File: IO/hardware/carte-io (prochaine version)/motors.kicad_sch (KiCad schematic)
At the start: 30 parts, among them J4 114020164, J5 114020164, J6 114020164, J7 114020164, J8 TSW-104-07-G-T, J9 TSW-104-07-G-T, U10 CM1293A-04SO, U11 74LVC125APW, U4 CM1293A-04SO, U5 TXU0104PWR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

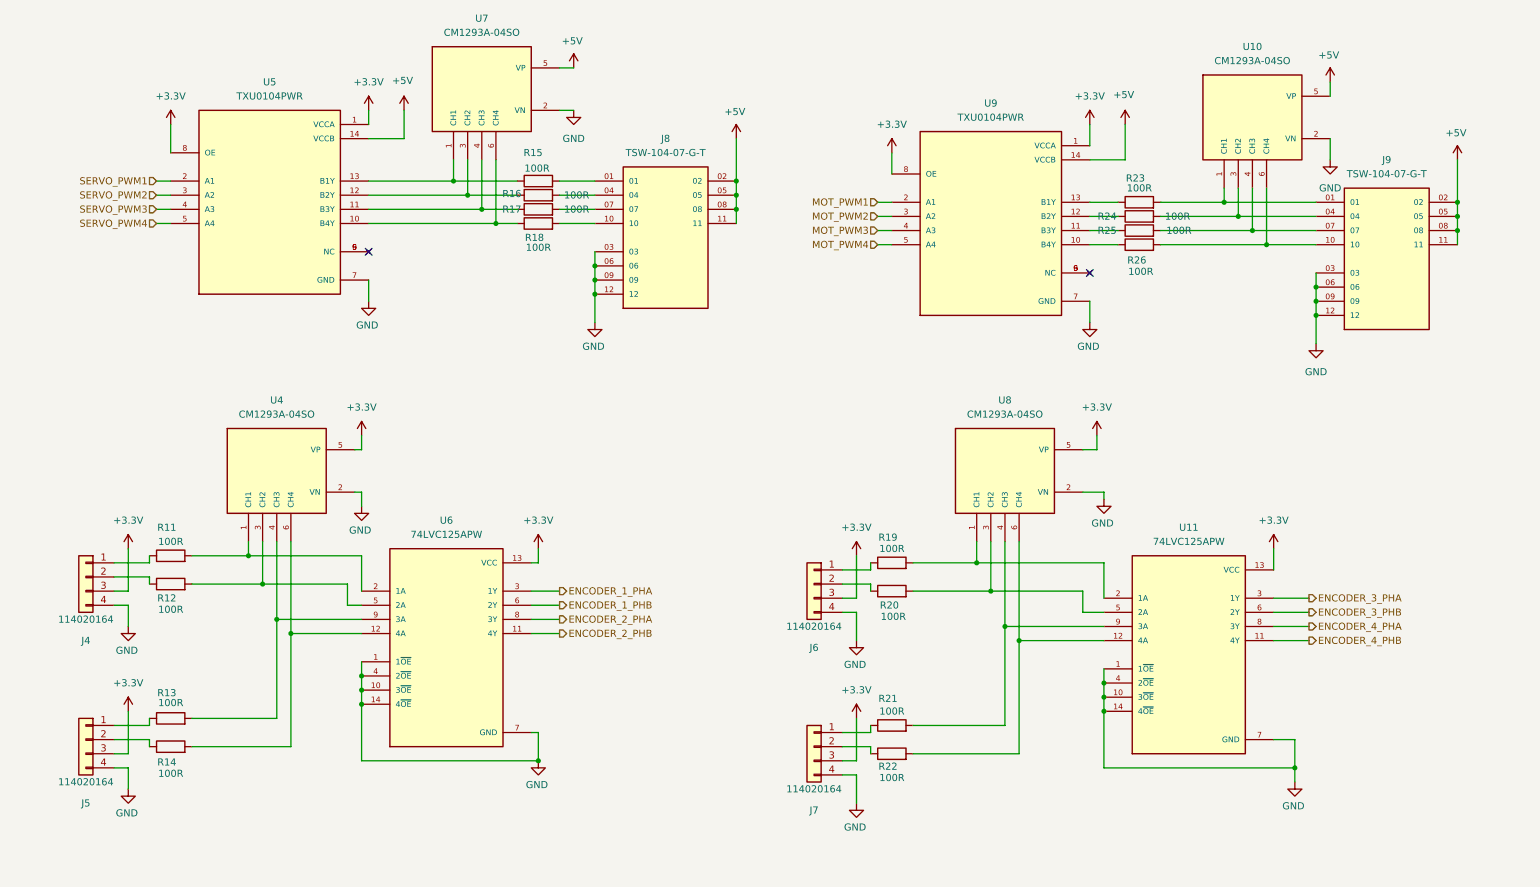
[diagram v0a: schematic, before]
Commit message: Recuperation de la carte IO perdue lors de la suppression des 3 derniers commit
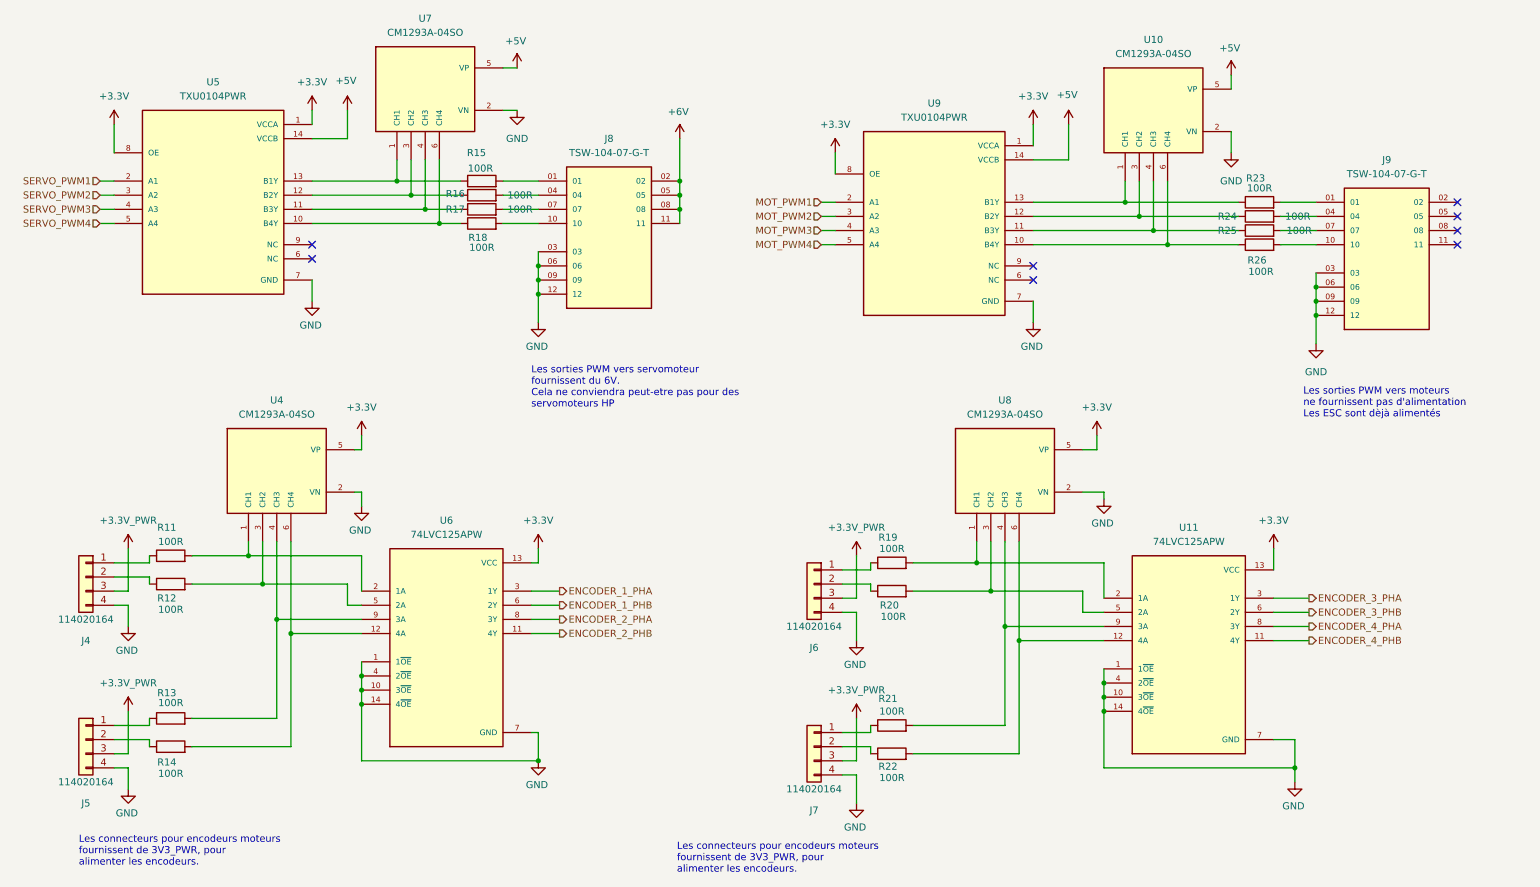
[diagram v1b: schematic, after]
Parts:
- U5, U9: Ref Manufacturer (none) -> TXU0104PWR
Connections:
- net +3.3V: no longer J4.3 (Pin_3), J5.3 (Pin_3), J6.3 (Pin_3), J7.3 (Pin_3)
- net +5V: no longer J8.02, J8.05, J8.08, J8.11, J9.02, J9.05, J9.08, J9.11
- net at R23.1, U9.13 (B1Y): now also U10.1 (CH1)
- net at J9.01, R23.2: no longer U10.1 (CH1)
- net at J9.04, R24.2: no longer U10.3 (CH2)
- net at J9.07, R25.2: no longer U10.4 (CH3)
- net at J9.10, R26.2: no longer U10.6 (CH4)
- net at R25.1, U9.11 (B3Y): now also U10.4 (CH3)
- net at R24.1, U9.12 (B2Y): now also U10.3 (CH2)
- net at R26.1, U9.10 (B4Y): now also U10.6 (CH4)
- net at U9.6 (NC): no longer U9.9 (NC)
- net at U5.6 (NC): no longer U5.9 (NC)
- new net +3.3V_PWR: J4.3 (Pin_3), J5.3 (Pin_3), J6.3 (Pin_3), J7.3 (Pin_3)
- new net +6V: J8.02, J8.05, J8.08, J8.11
- no-connect marks 2 -> 8
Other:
- note added: "Les connecteurs pour encodeurs moteurs fournissent de 3V3_PWR, pour alimenter les encodeurs."
- note added: "Les sorties PWM vers moteurs ne fournissent pas d'alimentation Les ESC sont dèjà alimentés"
- note added: "Les sorties PWM vers servomoteur fournissent du 6V. Cela ne conviendra peut-etre pas pour des servomoteurs HP"
- moved on the sheet: J8, R15, R16, R17, R18, R23, R24, R25, R26, U10, U5, U7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
